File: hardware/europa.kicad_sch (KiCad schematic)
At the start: 16 parts, among them J1 Left, J2 Right, J3 AudioJack2, J4 AudioJack2_Ground, J5 AudioJack2_Ground, J6 AudioJack2_Ground

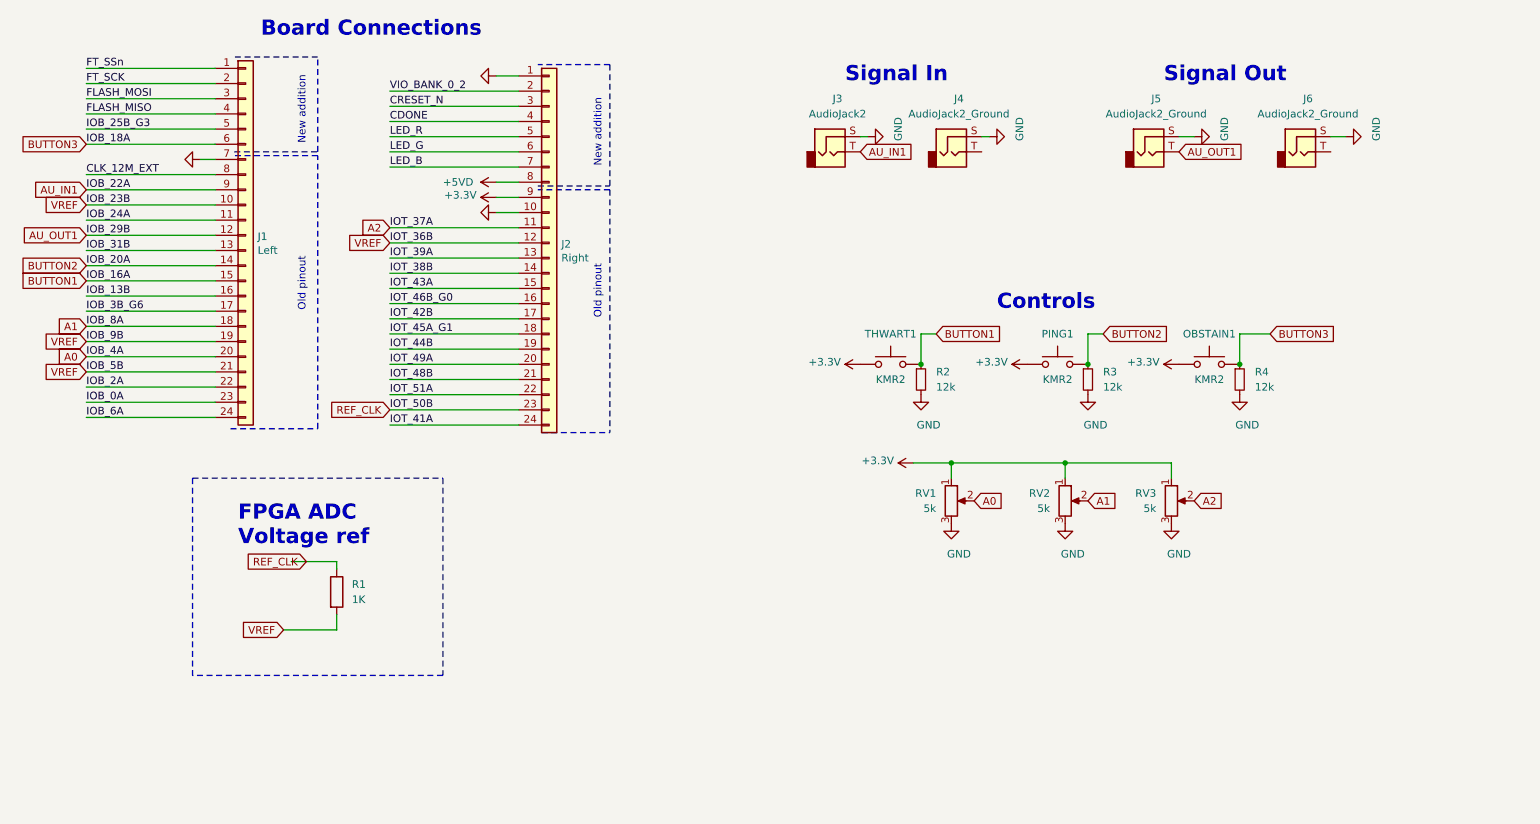
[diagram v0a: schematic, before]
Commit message: Europa 0.1, gerber files send to jlpcb. Added RTL reference design for adc.
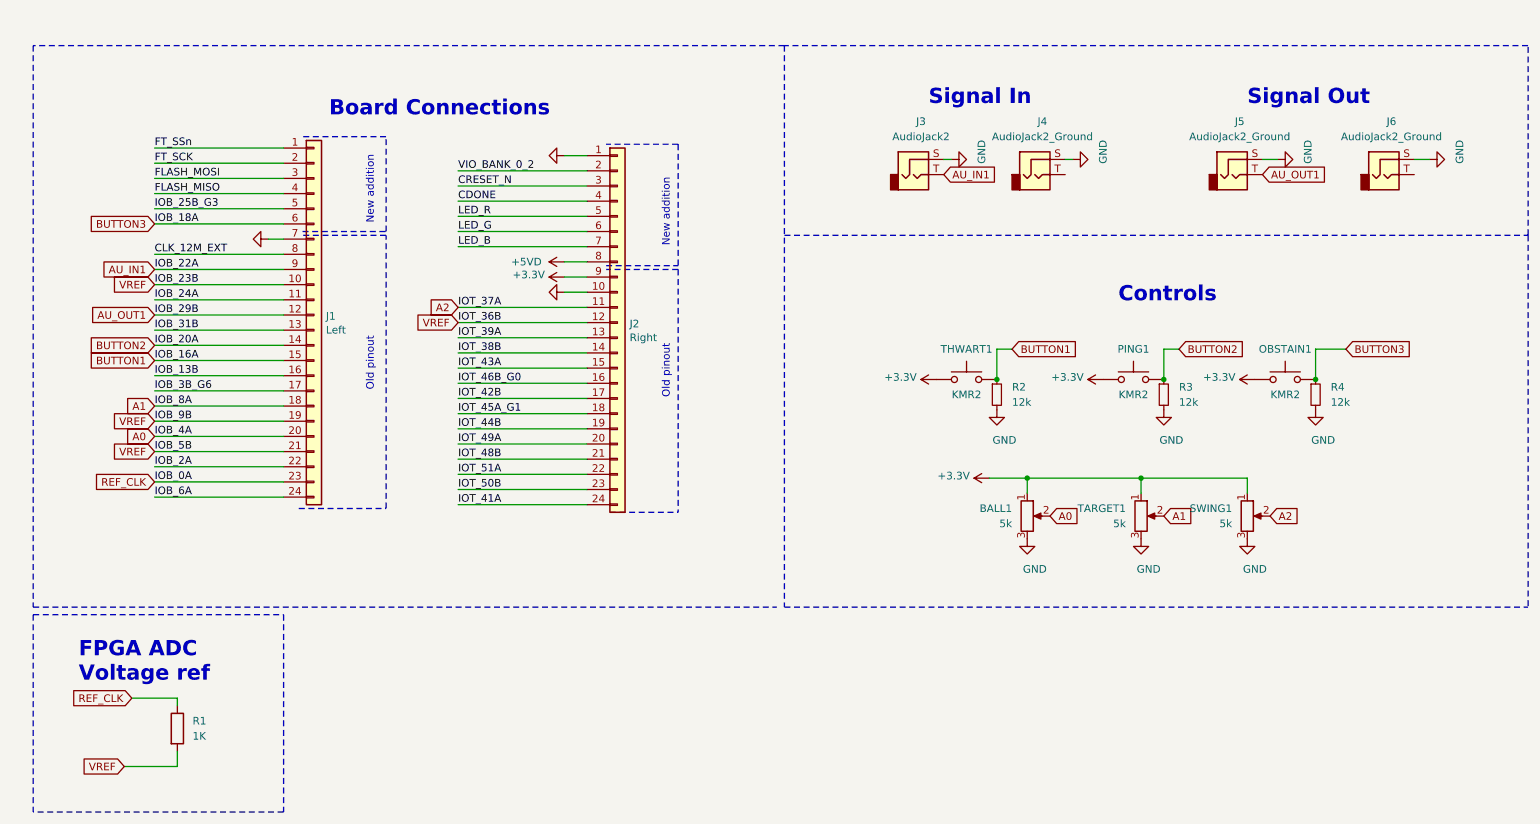
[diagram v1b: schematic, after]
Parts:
- renumbered RV1 to BALL1, RV3 to SWING1, RV2 to TARGET1
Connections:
- net IOB_0A is gone; now on net REF_CLK: J1.23 (Pin_23)
- net REF_CLK: no longer J2.23 (Pin_23)
- new net IOT_50B: J2.23 (Pin_23)
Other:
- moved on the sheet: BALL1, J1, J2, J3, J4, J5, J6, OBSTAIN1, PING1, R1, R2, R3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

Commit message: Sanitized hardware layout numbering, some silkscreen mods
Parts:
- added D1, D2: 3.3V, Diode_THT:D_DO-35_SOD27_P7.62mm_Horizontal, symbol Device:D_Zener_Small
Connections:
- net BUTTON3 is gone; now on net BUTTON2: J1.6 (Pin_6), OBSTAIN1.1, R4.1
- net IOT_50B is gone; now on net VREF: J2.23 (Pin_23)
- net IOT_51A is gone; now on net AU_IN1: J2.22 (Pin_22)
- net AU_IN1: now also J4.T, D2.1 (K); no longer J1.9 (Pin_9), J3.T
- net BUTTON1: now also J1.14 (Pin_14), PING1.1, R3.1; no longer J1.15 (Pin_15), R2.1, THWART1.1
- net BUTTON2: no longer J1.14 (Pin_14), PING1.1, R3.1
- net GND: now also D1.2 (A), D2.2 (A)
- net AU_OUT1 renamed AU_OUT0
- new net AU_IN0: D1.1 (K), J1.9 (Pin_9), J3.T
- new net BUTTON0: J1.15 (Pin_15), R2.1, THWART1.1
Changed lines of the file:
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@@
 (kicad_sch (version 20210126) (generator eeschema)
   (paper "A4")
+  (junction (at 167.64 40.64) (diameter 0.9144) (color 0 0 0 0))
   (junction (at 176.53 74.93) (diameter 0.9144) (color 0 0 0 0))
   (junction (at 181.61 91.44) (diameter 0.9144) (color 0 0 0 0))
+  (junction (at 187.96 40.64) (diameter 0.9144) (color 0 0 0 0))
   (junction (at 200.66 91.44) (diameter 0.9144) (color 0 0 0 0))
   (junction (at 204.47 74.93) (diameter 0.9144) (color 0 0 0 0))
@@
     (stroke (width 0) (type solid) (color 0 0 0 0))
   )
+  (wire (pts (xy 167.64 46.355) (xy 167.64 45.72))
+    (stroke (width 0) (type solid) (color 0 0 0 0))
+  )
   (wire (pts (xy 168.91 38.1) (xy 167.64 38.1))
     (stroke (width 0) (type solid) (color 0 0 0 0))
   )
+  (wire (pts (xy 168.91 40.64) (xy 167.64 40.64))
+    (stroke (width 0) (type solid) (color 0 0 0 0))
+  )
   (wire (pts (xy 175.26 91.44) (xy 181.61 91.44))
     (stroke (width 0) (type solid) (color 0 0 0 0))
@@
   )
   (wire (pts (xy 181.61 91.44) (xy 200.66 91.44))
+    (stroke (width 0) (type solid) (color 0 0 0 0))
+  )
+  (wire (pts (xy 187.96 40.64) (xy 189.23 40.64))
+    (stroke (width 0) (type solid) (color 0 0 0 0))
+  )
+  (wire (pts (xy 187.96 46.355) (xy 187.96 45.72))
     (stroke (width 0) (type solid) (color 0 0 0 0))
   )
@@
     )
   )
-  (global_label "BUTTON3" (shape input) (at 35.56 48.895 180)
+  (global_label "BUTTON2" (shape input) (at 35.56 48.895 180)
     (effects (font (size 1.27 1.27)) (justify right))
     (property "Intersheet References" "${INTERSHEET_REFS}" (id 0) (at 24.7407 48.8156 0)
@@
     )
   )
-  (global_label "AU_IN1" (shape input) (at 35.56 56.515 180)
-    (effects (font (size 1.27 1.27)) (justify right))
-    (property "Intersheet References" "${INTERSHEET_REFS}" (id 0) (at 26.6155 56.5944 0)
+  (global_label "AU_IN0" (shape input) (at 35.56 56.515 180)
+    (effects (font (size 1.27 1.27)) (justify right))
+    (property "Intersheet References" "${INTERSHEET_REFS}" (id 0) (at 26.6155 56.4356 0)
       (effects (font (size 1.27 1.27)) (justify right) hide)
     )
@@
     )
   )
-  (global_label "AU_OUT1" (shape input) (at 35.56 64.135 180)
-    (effects (font (size 1.27 1.27)) (justify right))
-    (property "Intersheet References" "${INTERSHEET_REFS}" (id 0) (at 24.9221 64.2144 0)
-      (effects (font (size 1.27 1.27)) (justify right) hide)
-    )
-  )
-  (global_label "BUTTON2" (shape input) (at 35.56 69.215 180)
+  (global_label "AU_OUT0" (shape input) (at 35.56 64.135 180)
+    (effects (font (size 1.27 1.27)) (justify right))
+    (property "Intersheet References" "${INTERSHEET_REFS}" (id 0) (at 24.9221 64.0556 0)
+      (effects (font (size 1.27 1.27)) (justify right) hide)
+    )
+  )
+  (global_label "BUTTON1" (shape input) (at 35.56 69.215 180)
     (effects (font (size 1.27 1.27)) (justify right))
     (property "Intersheet References" "${INTERSHEET_REFS}" (id 0) (at 24.7407 69.1356 0)
@@
     )
   )
-  (global_label "BUTTON1" (shape input) (at 35.56 71.755 180)
-    (effects (font (size 1.27 1.27)) (justify right))
-    (property "Intersheet References" "${INTERSHEET_REFS}" (id 0) (at 24.7407 71.8344 0)
+  (global_label "BUTTON0" (shape input) (at 35.56 71.755 180)
+    (effects (font (size 1.27 1.27)) (justify right))
+    (property "Intersheet References" "${INTERSHEET_REFS}" (id 0) (at 24.7407 71.6756 0)
       (effects (font (size 1.27 1.27)) (justify right) hide)
     )
@@
     )
   )
-  (global_label "AU_IN1" (shape input) (at 167.64 40.64 0)
+  (global_label "AU_IN1" (shape input) (at 86.36 90.805 180)
+    (effects (font (size 1.27 1.27)) (justify right))
+    (property "Intersheet References" "${INTERSHEET_REFS}" (id 0) (at 77.4155 90.7256 0)
+      (effects (font (size 1.27 1.27)) (justify right) hide)
+    )
+  )
+  (global_label "VREF" (shape input) (at 86.36 93.345 180)
+    (effects (font (size 1.27 1.27)) (justify right))
+    (property "Intersheet References" "${INTERSHEET_REFS}" (id 0) (at 79.3507 93.2656 0)
+      (effects (font (size 1.27 1.27)) (justify right) hide)
+    )
+  )
+  (global_label "AU_IN0" (shape input) (at 168.91 40.64 0)
     (effects (font (size 1.27 1.27)) (justify left))
-    (property "Intersheet References" "${INTERSHEET_REFS}" (id 0) (at 176.5845 40.5606 0)
+    (property "Intersheet References" "${INTERSHEET_REFS}" (id 0) (at 177.8545 40.5606 0)
       (effects (font (size 1.27 1.27)) (justify left) hide)
     )
   )
-  (global_label "BUTTON1" (shape input) (at 179.07 69.85 0)
+  (global_label "BUTTON0" (shape input) (at 179.07 69.85 0)
     (effects (font (size 1.27 1.27)) (justify left))
     (property "Intersheet References" "${INTERSHEET_REFS}" (id 0) (at 189.8893 69.7706 0)
@@
     )
   )
+  (global_label "AU_IN1" (shape input) (at 189.23 40.64 0)
+    (effects (font (size 1.27 1.27)) (justify left))
+    (property "Intersheet References" "${INTERSHEET_REFS}" (id 0) (at 198.1745 40.5606 0)
+      (effects (font (size 1.27 1.27)) (justify left) hide)
+    )
+  )
   (global_label "A1" (shape input) (at 204.47 97.79 0)
     (effects (font (size 1.27 1.27)) (justify left))
@@
     )
   )
-  (global_label "BUTTON2" (shape input) (at 207.01 69.85 0)
+  (global_label "BUTTON1" (shape input) (at 207.01 69.85 0)
     (effects (font (size 1.27 1.27)) (justify left))
     (property "Intersheet References" "${INTERSHEET_REFS}" (id 0) (at 217.8293 69.7706 0)
@@
     )
   )
-  (global_label "AU_OUT1" (shape input) (at 220.98 40.64 0)
+  (global_label "AU_OUT0" (shape input) (at 220.98 40.64 0)
     (effects (font (size 1.27 1.27)) (justify left))
     (property "Intersheet References" "${INTERSHEET_REFS}" (id 0) (at 231.6179 40.5606 0)
@@
     )
   )
-  (global_label "BUTTON3" (shape input) (at 234.95 69.85 0)
+  (global_label "BUTTON2" (shape input) (at 234.95 69.85 0)
     (effects (font (size 1.27 1.27)) (justify left))
     (property "Intersheet References" "${INTERSHEET_REFS}" (id 0) (at 245.7693 69.7706 0)
@@
     (pin "1")
   )
+  (symbol (lib_id "power:GND") (at 167.64 46.355 0) (unit 1)
+    (in_bom yes) (on_board yes)
+    (property "Reference" "#PWR0121" (id 0) (at 167.64 52.705 0)
+      (effects (font (size 1.27 1.27)) hide)
+    )
+    (property "Value" "GND" (id 1) (at 168.91 51.435 0))
+    (property "Footprint" "" (id 2) (at 167.64 46.355 0)
+      (effects (font (size 1.27 1.27)) hide)
+    )
+    (property "Datasheet" "" (id 3) (at 167.64 46.355 0)
+      (effects (font (size 1.27 1.27)) hide)
+    )
+    (pin "1")
+  )
   (symbol (lib_id "power:GND") (at 168.91 38.1 90) (unit 1)
     (in_bom yes) (on_board yes)
@@
     (pin "1")
   )
+  (symbol (lib_id "power:GND") (at 187.96 46.355 0) (unit 1)
+    (in_bom yes) (on_board yes)
+    (property "Reference" "#PWR0120" (id 0) (at 187.96 52.705 0)
+      (effects (font (size 1.27 1.27)) hide)
+    )
+    (property "Value" "GND" (id 1) (at 189.23 51.435 0))
+    (property "Footprint" "" (id 2) (at 187.96 46.355 0)
+      (effects (font (size 1.27 1.27)) hide)
+    )
+    (property "Datasheet" "" (id 3) (at 187.96 46.355 0)
+      (effects (font (size 1.27 1.27)) hide)
+    )
+    (pin "1")
+  )
   (symbol (lib_id "power:GND") (at 189.23 38.1 90) (unit 1)
     (in_bom yes) (on_board yes)
@@
     )
     (property "Datasheet" "~" (id 3) (at 229.87 77.47 0)
+      (effects (font (size 1.27 1.27)) hide)
+    )
+    (pin "1")
+    (pin "2")
+  )
+  (symbol (lib_id "Device:D_Zener_Small") (at 167.64 43.18 270) (unit 1)
+    (in_bom yes) (on_board yes)
+    (property "Reference" "D1" (id 0) (at 170.18 41.91 90)
+      (effects (font (size 1.27 1.27)) (justify left))
+    )
+    (property "Value" "3.3V" (id 1) (at 170.18 44.45 90)
+      (effects (font (size 1.27 1.27)) (justify left))
+    )
+    (property "Footprint" "Diode_THT:D_DO-35_SOD27_P7.62mm_Horizontal" (id 2) (at 167.64 43.18 90)
+      (effects (font (size 1.27 1.27)) hide)
+    )
+    (property "Datasheet" "~" (id 3) (at 167.64 43.18 90)
+      (effects (font (size 1.27 1.27)) hide)
+    )
+    (pin "1")
+    (pin "2")
+  )
+  (symbol (lib_id "Device:D_Zener_Small") (at 187.96 43.18 270) (unit 1)
+    (in_bom yes) (on_board yes)
+    (property "Reference" "D2" (id 0) (at 189.865 41.91 90)
+      (effects (font (size 1.27 1.27)) (justify left))
+    )
+    (property "Value" "3.3V" (id 1) (at 189.865 44.45 90)
+      (effects (font (size 1.27 1.27)) (justify left))
+    )
+    (property "Footprint" "Diode_THT:D_DO-35_SOD27_P7.62mm_Horizontal" (id 2) (at 187.96 43.18 90)
+      (effects (font (size 1.27 1.27)) hide)
+    )
+    (property "Datasheet" "~" (id 3) (at 187.96 43.18 90)
       (effects (font (size 1.27 1.27)) hide)
     )
@@
       (reference "#PWR0119") (unit 1) (value "GND") (footprint "")
     )
+    (path "/cef0caa0-9ec0-40b1-8988-b9aa0d78ab89"
+      (reference "#PWR0120") (unit 1) (value "GND") (footprint "")
+    )
+    (path "/200623ef-47eb-46bd-8746-7815e7c73536"
+      (reference "#PWR0121") (unit 1) (value "GND") (footprint "")
+    )
     (path "/523368eb-02d7-44e1-959d-d8e13910a358"
       (reference "BALL1") (unit 1) (value "5k") (footprint "Potentiometer_THT:Potentiometer_Alps_RK09K_Single_Vertical")
     )
+    (path "/f5db0e98-4d7e-4985-a282-0e5b1688c5ee"
+      (reference "D1") (unit 1) (value "3.3V") (footprint "Diode_THT:D_DO-35_SOD27_P7.62mm_Horizontal")
+    )
+    (path "/0f061700-8f13-465f-8a1d-963f3f090198"
+      (reference "D2") (unit 1) (value "3.3V") (footprint "Diode_THT:D_DO-35_SOD27_P7.62mm_Horizontal")
+    )
     (path "/9054d683-879e-4cd8-97c5-c9796ad59584"

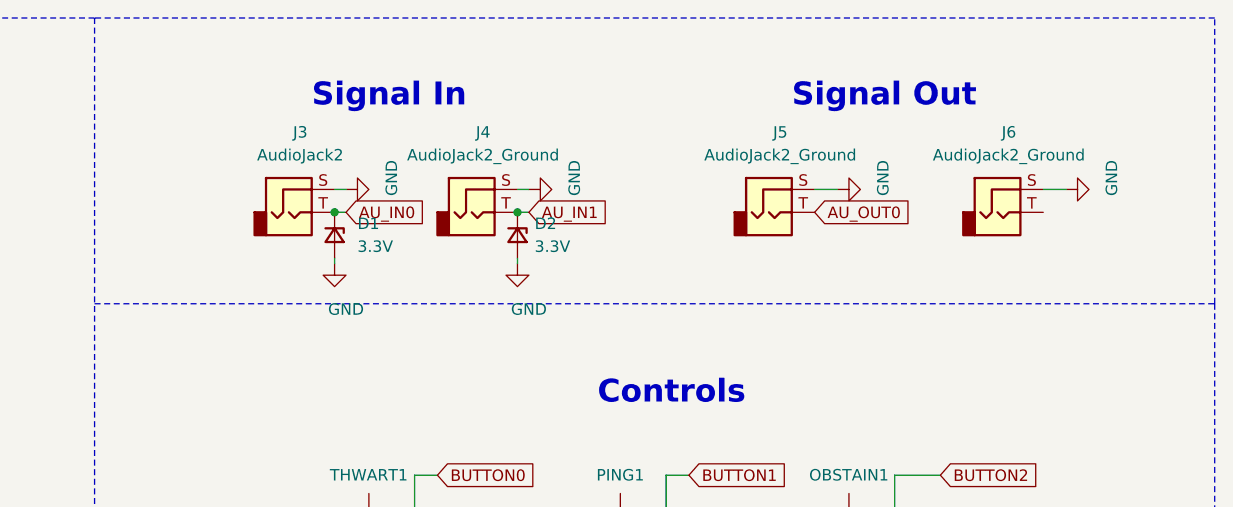
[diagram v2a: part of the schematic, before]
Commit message: Added zener diode series resistor for 5V TTL
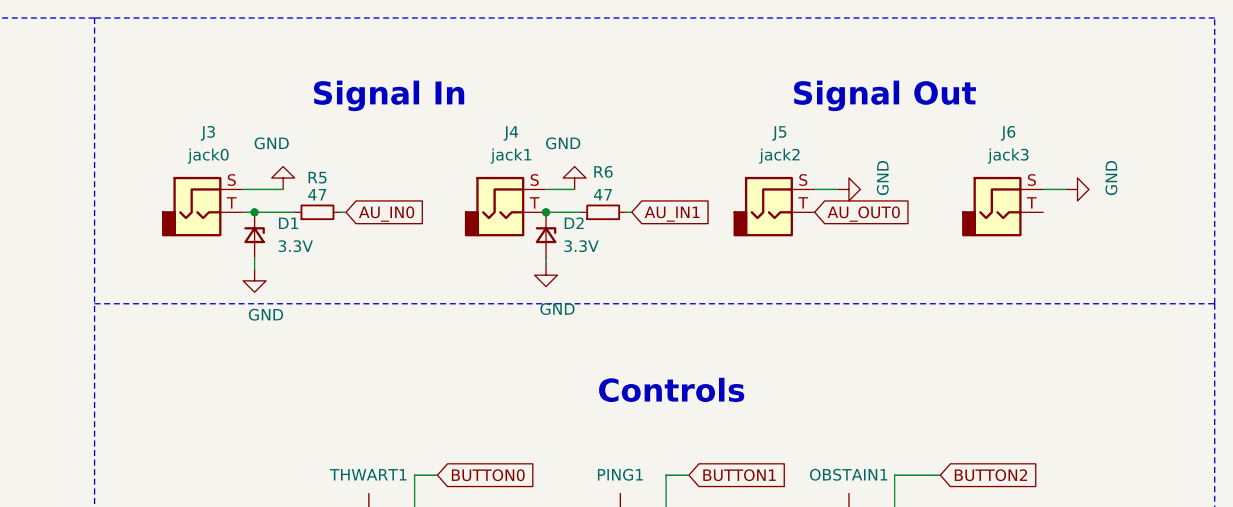
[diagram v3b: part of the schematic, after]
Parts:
- added R5, R6: 47, symbol Device:R_Small
- J3: value AudioJack2 -> jack0
- J4: value AudioJack2_Ground -> jack1
- J5: value AudioJack2_Ground -> jack2
- J6: value AudioJack2_Ground -> jack3
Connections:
- net AU_IN0: now also R5.2; no longer D1.1 (K), J3.T
- net AU_IN1: now also R6.2; no longer D2.1 (K), J4.T
- new net: D2.1 (K), J4.T, R6.1
- new net: D1.1 (K), J3.T, R5.1
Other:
- moved on the sheet: D1, D2, J3, J4
